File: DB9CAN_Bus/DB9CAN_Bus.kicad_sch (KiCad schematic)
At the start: 10 parts, among them J1 DE9_Receptacle, J10 DE9_Receptacle, J2 DE9_Receptacle, J3 DE9_Receptacle, J4 DE9_Receptacle, J5 DE9_Receptacle, J6 DE9_Receptacle, J7 DE9_Receptacle, J8 DE9_Receptacle, J9 DE9_Receptacle

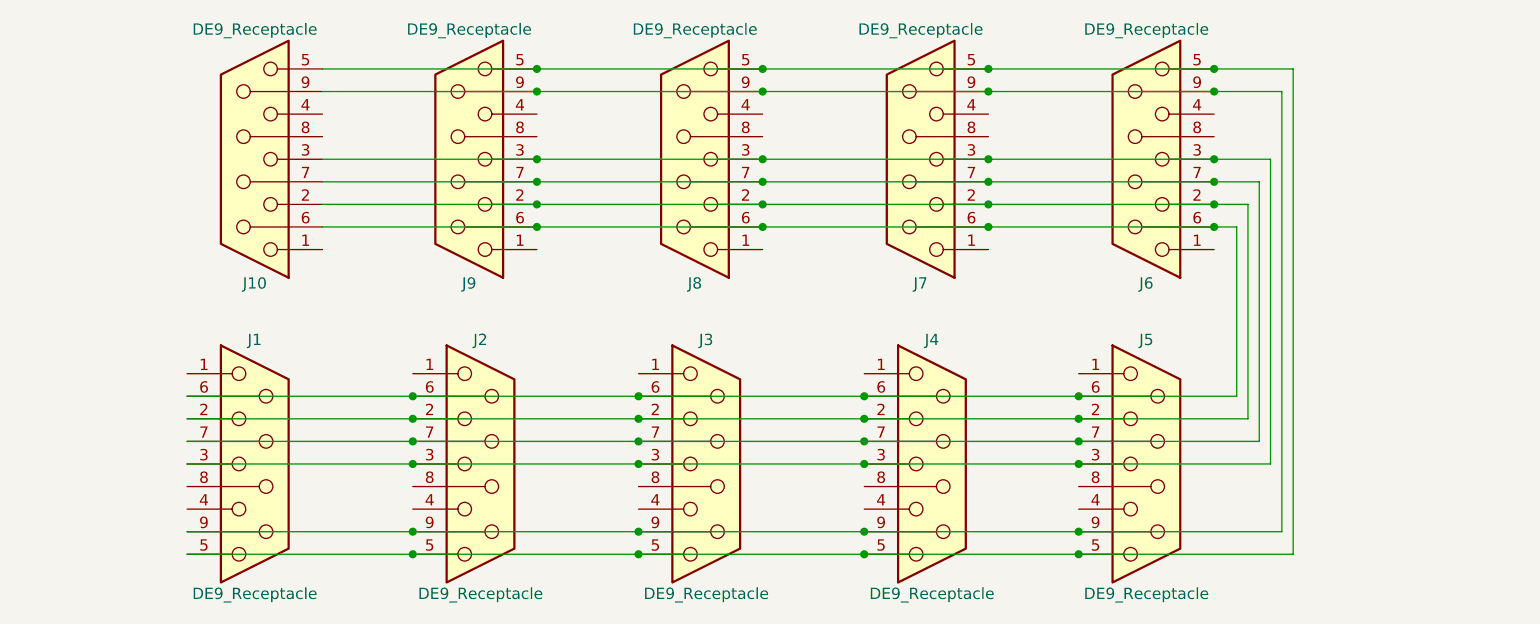
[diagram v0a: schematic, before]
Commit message: Split the AOA LED project into two projects - one for the LEDs and one for the Nano board and the MCP2515 CAN board.
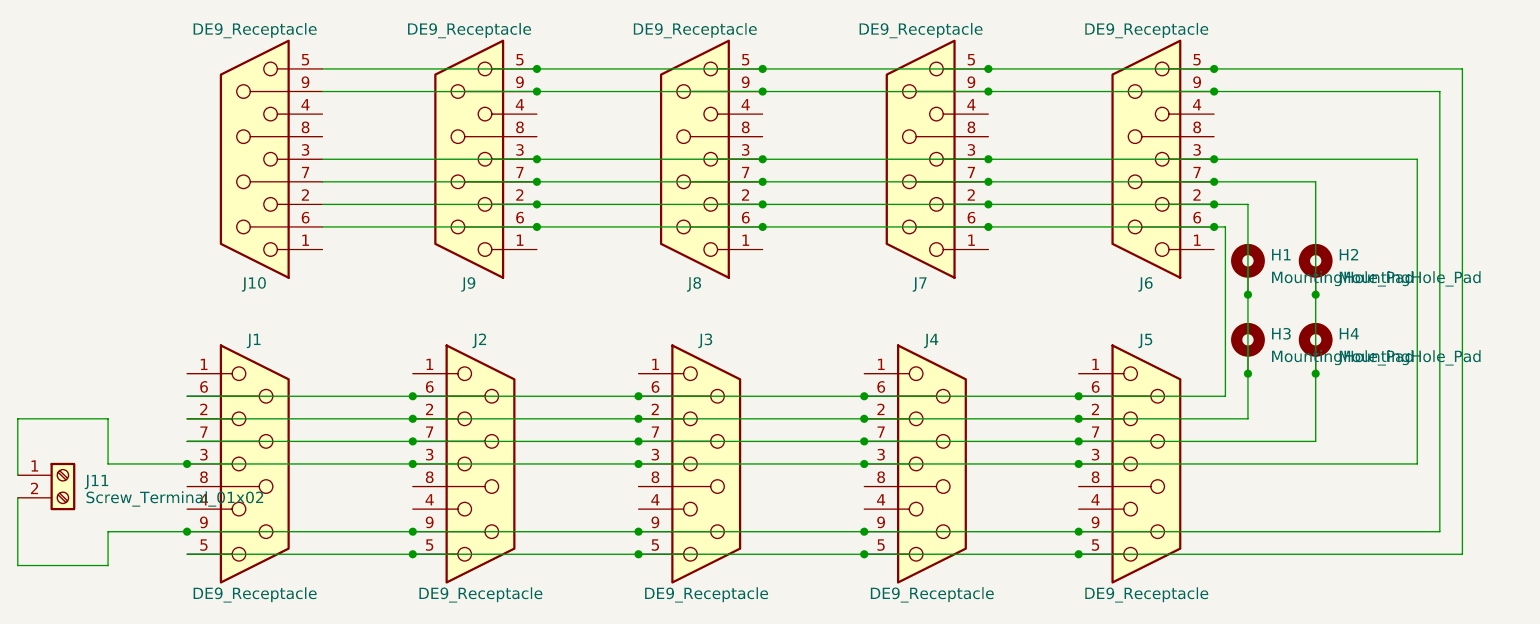
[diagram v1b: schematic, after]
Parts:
- added H1, H2, H3, H4: MountingHole_Pad, MountingHole:MountingHole_2.2mm_M2_DIN965_Pad, symbol Mechanical:MountingHole_Pad
- added J11: Screw_Terminal_01x02, TerminalBlock:TerminalBlock_bornier-2_P5.08mm, symbol Connector:Screw_Terminal_01x02
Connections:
- net at J1.2, J10.2, J2.2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: now also H1.1, H3.1
- net at J1.3, J10.3, J2.3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: now also J11.1 (Pin_1)
- net at J1.7, J10.7, J2.7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: now also H2.1, H4.1
- net at J1.9, J10.9, J2.9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: now also J11.2 (Pin_2)
